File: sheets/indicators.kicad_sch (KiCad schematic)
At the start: 18 parts, among them Q3 AO3400A

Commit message: Fixed up power, added remaining to do
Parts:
- D7: value USB LED -> SERVO LED
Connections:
- net 12V: no longer names the net of D8.2 (A)
- net 3V3: no longer names the net of D4.2 (A)
- net 3V3: no longer D5.2 (A)
- net 5V renamed +5V
- net 5V SERVO: no longer names the net of D7.2 (A)
- new net +3V3: D5.2 (A)
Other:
- note added: "todo: decide on a GPIO pin for LED"
- note added: "todo: make a +7.4V_SERVO power symbol and stick here"
- moved on the sheet: D6, D8, R21, R23

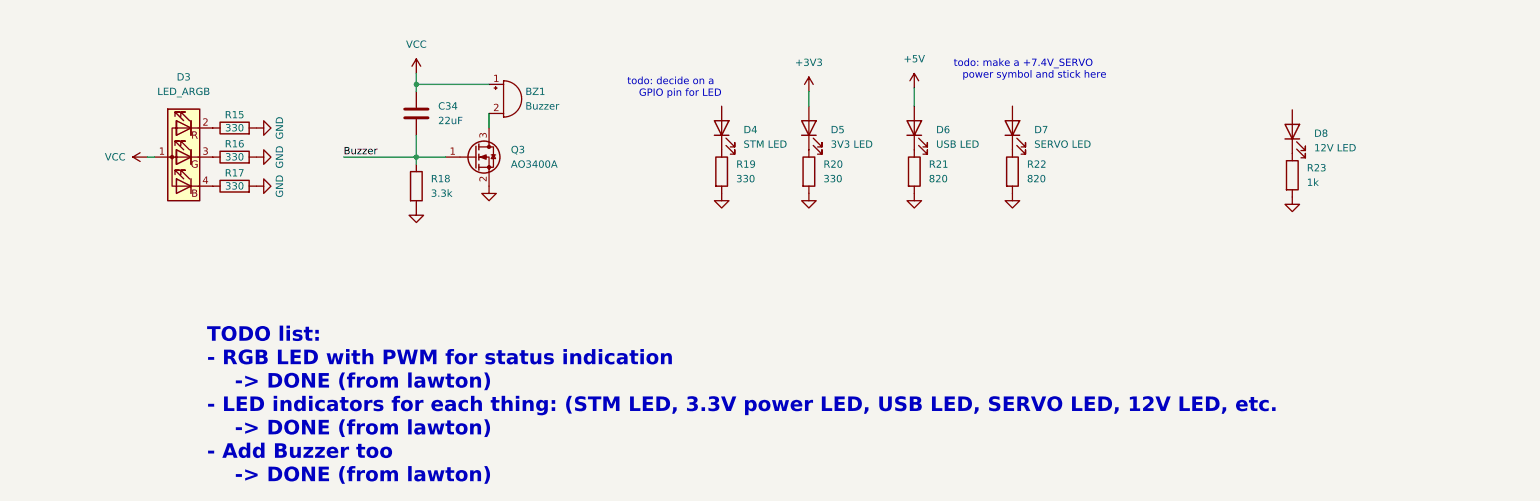
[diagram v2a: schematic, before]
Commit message: polished up circuit, added new 16.8V to 7.4V step down circuit components
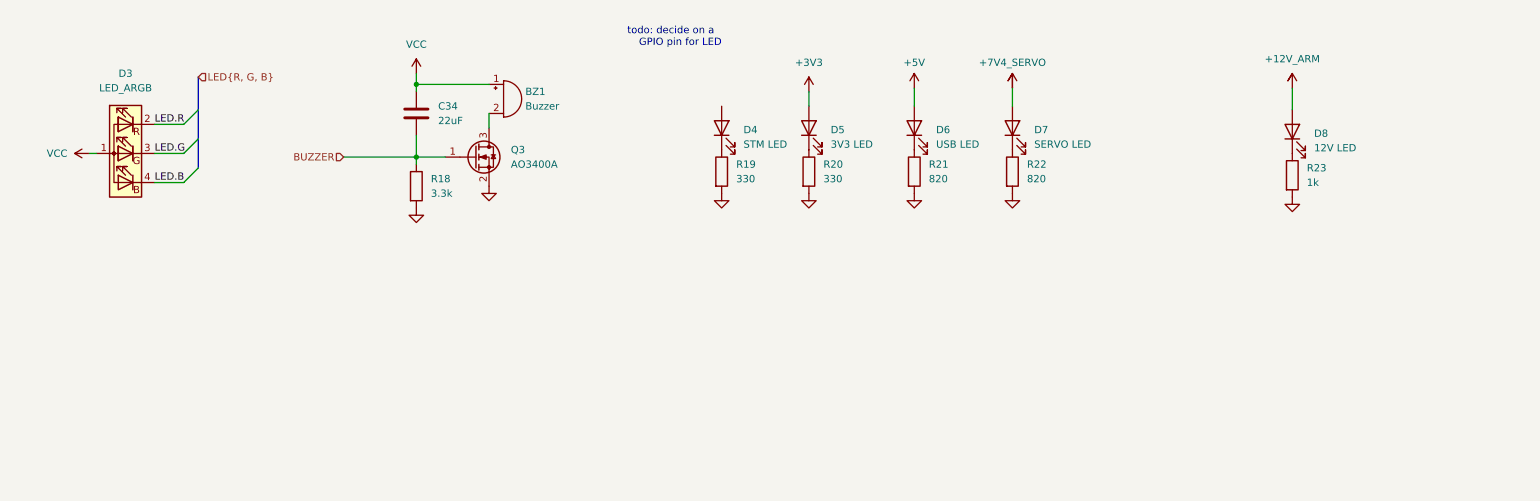
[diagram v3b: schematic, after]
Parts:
- removed R15, R16, R17: 330, symbol Device:R
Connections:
- net LED.G: now reaches D3.3 (GK)
- net +7V4_SERVO: now reaches D7.2 (A)
- net LED.B: now reaches D3.4 (BK)
- net +12V_ARM: now reaches D8.2 (A)
- net LED.R: now reaches D3.2 (RK)
- net Buzzer renamed BUZZER
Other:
- note removed: "TODO list: - RGB LED with PWM for status indication -> DONE (from lawton) - LED indicators for each thing: (STM LED, 3.3V power LED, USB LED, SERVO LED, 12V LED, etc. -> DONE (from lawton) - Add Buzzer too -> DONE (from lawton)"
- note removed: "todo: make a +7.4V_SERVO power symbol and stick here"
- moved on the sheet: D3

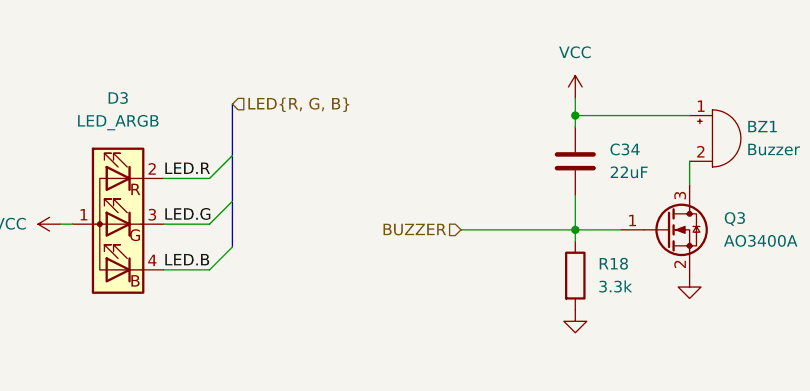
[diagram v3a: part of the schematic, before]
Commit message: led pwm
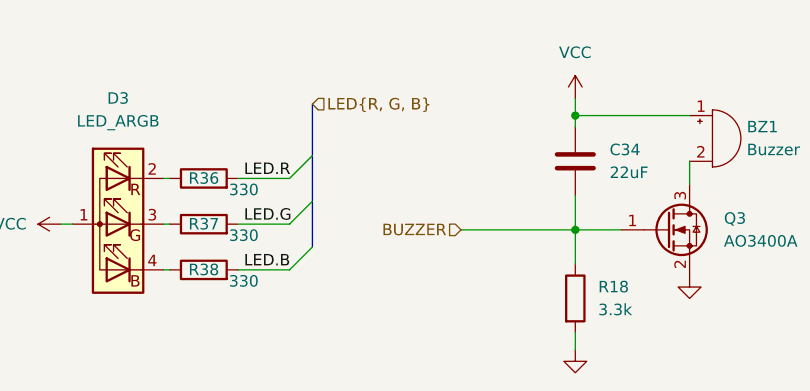
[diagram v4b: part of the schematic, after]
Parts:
- added R36, R37, R38: 330, symbol Device:R
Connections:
- net LED.B: now also R38.2; no longer D3.4 (BK)
- net LED.G: now also R37.2; no longer D3.3 (GK)
- net LED.R: now also R36.2; no longer D3.2 (RK)
- new net: D3.4 (BK), R38.1
- new net: D3.2 (RK), R36.1
- new net: D3.3 (GK), R37.1
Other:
- moved on the sheet: R18

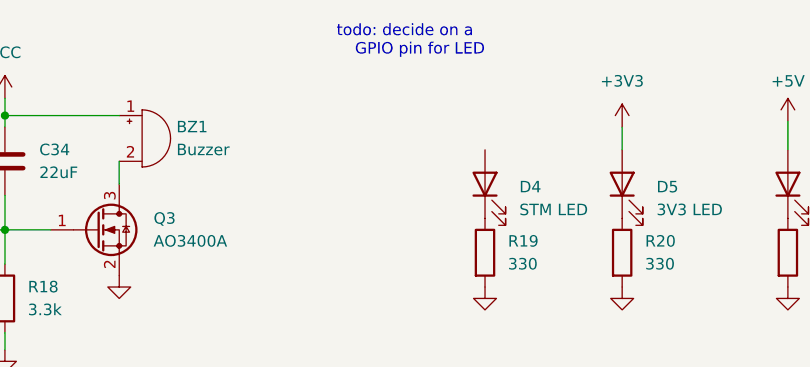
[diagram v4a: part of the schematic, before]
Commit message: assigned gpio pin to led (pg6)
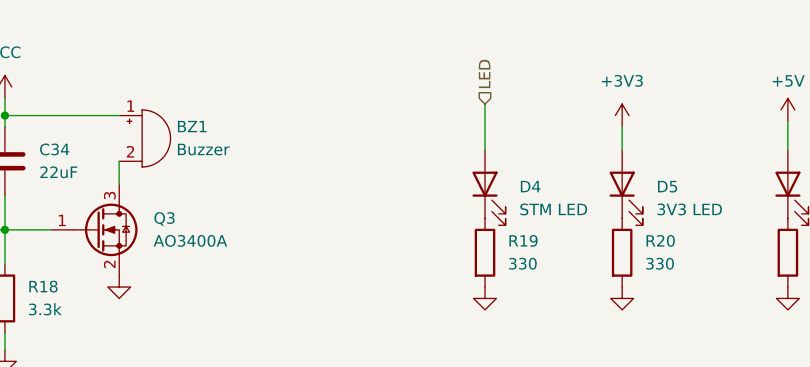
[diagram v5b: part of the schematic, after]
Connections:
- net LED: now reaches D4.2 (A)
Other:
- note removed: "todo: decide on a GPIO pin for LED"
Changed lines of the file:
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@@
 	(generator_version "9.0")
 	(paper "A4")
-	(text "todo: decide on a \n	  GPIO pin for LED\n"
-		(exclude_from_sim no)
-		(at 127 22.225 0)
-		(effects
-			(font
-				(size 1.27 1.27)
-			)
-		)
-	)
 	(junction
 		(at 82.55 43.18)
@@
 	(wire
 		(pts
+			(xy 135.89 29.21) (xy 135.89 34.29)
+		)
+		(stroke
+			(width 0)
+			(type default)
+		)
+	)
+	(wire
+		(pts
 			(xy 45.085 47.625) (xy 50.8 47.625)
 		)
@@
 		)
 	)
+	(hierarchical_label "LED"
+		(shape input)
+		(at 135.89 29.21 90)
+		(effects
+			(font
+				(size 1.27 1.27)
+			)
+			(justify left)
+		)
+	)

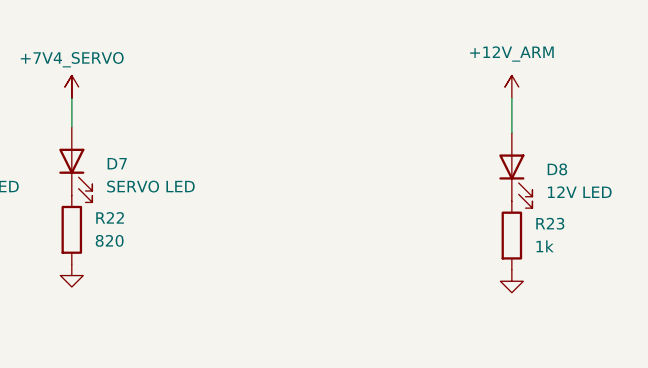
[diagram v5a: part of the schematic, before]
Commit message: added gpio connections in root, UART8, ADC2
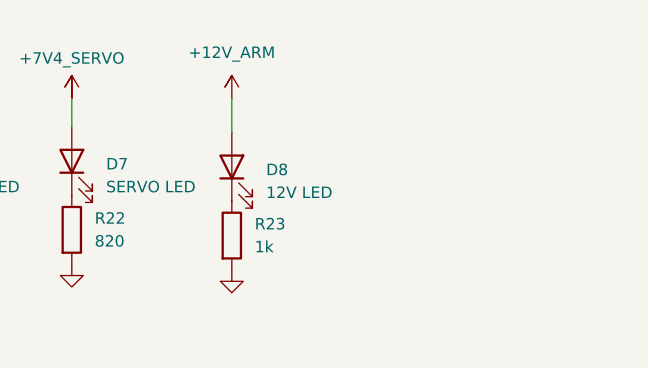
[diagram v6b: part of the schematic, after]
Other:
- moved on the sheet: D8, R23
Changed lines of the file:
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@@
 	(wire
 		(pts
-			(xy 235.585 31.115) (xy 235.585 34.925)
+			(xy 204.47 31.115) (xy 204.47 34.925)
 		)
 		(stroke
@@
 	(symbol
 		(lib_id "Device:R")
-		(at 235.585 46.355 0)
+		(at 204.47 46.355 0)
 		(unit 1)
 		(exclude_from_sim no)
@@
 		(fields_autoplaced yes)
 		(property "Reference" "R23"
-			(at 238.125 45.0849 0)
+			(at 207.01 45.0849 0)
 			(effects
 				(font
@@
 		)
 		(property "Value" "1k"
-			(at 238.125 47.6249 0)
+			(at 207.01 47.6249 0)
 			(effects
 				(font
@@
 		)
 		(property "Footprint" ""
-			(at 233.807 46.355 90)
+			(at 202.692 46.355 90)
 			(effects
 				(font
@@
 		)
 		(property "Datasheet" "~"
-			(at 235.585 46.355 0)
+			(at 204.47 46.355 0)
 			(effects
 				(font
@@
 		)
 		(property "Description" "Resistor"
-			(at 235.585 46.355 0)
+			(at 204.47 46.355 0)
 			(effects
 				(font
@@
 	(symbol
 		(lib_id "aerolotl_custom:+12V_ARM")
-		(at 235.585 31.115 0)
+		(at 204.47 31.115 0)
 		(unit 1)
 		(exclude_from_sim no)
@@
 		(fields_autoplaced yes)
 		(property "Reference" "#PWR097"
-			(at 235.585 31.115 0)
+			(at 204.47 31.115 0)
 			(effects
 				(font
@@
 		)
 		(property "Value" "+12V_ARM"
-			(at 235.585 26.035 0)
-			(effects
-				(font
-					(size 1.27 1.27)
-				)
-			)
-		)
-		(property "Footprint" ""
-			(at 235.585 31.115 0)
+			(at 204.47 26.035 0)
+			(effects
+				(font
+					(size 1.27 1.27)
+				)
+			)
+		)
+		(property "Footprint" ""
+			(at 204.47 31.115 0)
 			(effects
 				(font
@@
 		)
 		(property "Datasheet" ""
-			(at 235.585 31.115 0)
+			(at 204.47 31.115 0)
 			(effects
 				(font
@@
 		)
 		(property "Description" ""
-			(at 235.585 31.115 0)
+			(at 204.47 31.115 0)
 			(effects
 				(font
@@
 	(symbol
 		(lib_id "Device:LED")
-		(at 235.585 38.735 90)
+		(at 204.47 38.735 90)
 		(unit 1)
 		(exclude_from_sim no)
@@
 		(fields_autoplaced yes)
 		(property "Reference" "D8"
-			(at 239.395 39.0524 90)
+			(at 208.28 39.0524 90)
 			(effects
 				(font
@@
 		)
 		(property "Value" "12V LED"
-			(at 239.395 41.5924 90)
+			(at 208.28 41.5924 90)
 			(effects
 				(font
@@
 		)
 		(property "Footprint" ""
-			(at 235.585 38.735 0)
+			(at 204.47 38.735 0)
 			(effects
 				(font
@@
 		)
 		(property "Datasheet" "~"
-			(at 235.585 38.735 0)
+			(at 204.47 38.735 0)
 			(effects
 				(font
@@
 		)
 		(property "Description" "Light emitting diode"
-			(at 235.585 38.735 0)
+			(at 204.47 38.735 0)
 			(effects
 				(font
@@
 		)
 		(property "Sim.Pins" "1=K 2=A"
-			(at 235.585 38.735 0)
+			(at 204.47 38.735 0)
 			(effects
 				(font
@@
 	(symbol
 		(lib_id "power:GND")
-		(at 235.585 50.165 0)
+		(at 204.47 50.165 0)
 		(unit 1)
 		(exclude_from_sim no)
@@
 		(fields_autoplaced yes)
 		(property "Reference" "#PWR079"
-			(at 235.585 56.515 0)
+			(at 204.47 56.515 0)
 			(effects
 				(font
@@
 		)
 		(property "Value" "GND"
-			(at 235.585 55.245 0)
-			(effects
-				(font
-					(size 1.27 1.27)
-				)
-				(hide yes)
-			)
-		)
-		(property "Footprint" ""
-			(at 235.585 50.165 0)
+			(at 204.47 55.245 0)
+			(effects
+				(font
+					(size 1.27 1.27)
+				)
+				(hide yes)
+			)
+		)
+		(property "Footprint" ""
+			(at 204.47 50.165 0)
 			(effects
 				(font
@@
 		)
 		(property "Datasheet" ""
-			(at 235.585 50.165 0)
+			(at 204.47 50.165 0)
 			(effects
 				(font
@@
 		)
 		(property "Description" "Power symbol creates a global label with name \"GND\" , ground"
-			(at 235.585 50.165 0)
-			(effects
-				(font
+			(at 204.47 50.165 0)
+			(effects
+				(font

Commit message: Rev1 schematic done
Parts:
- renumbered C34 to C44, D3 to D1, D4 to D2, D5 to D3, D6 to D4, D7 to D5, D8 to D6, Q3 to Q1, R36 to R19, R37 to R20, R38 to R21, R18 to R22, R19 to R23, R20 to R24, R21 to R25, R22 to R26, R23 to R27
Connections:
- net VCC is gone; now on net +3V3: BZ1.1 (+), C44.1, D1.1 (A)
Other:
- moved on the sheet: BZ1, C44, D1, D2, D3, D4, D5, D6, Q1, R19, R20, R21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

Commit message: Cleared all ERC errors
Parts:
- BZ1: footprint (none) -> aerolotl_custom:BUZ-TH_BD12.0-P6.50-D0.6-FD
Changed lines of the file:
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@@
 			)
 		)
-		(property "Footprint" ""
+		(property "Footprint" "aerolotl_custom:BUZ-TH_BD12.0-P6.50-D0.6-FD"
 			(at 106.045 27.94 90)
 			(effects
